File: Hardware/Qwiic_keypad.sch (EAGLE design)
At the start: 26 parts, among them J3 PTH, J6 AVR_SPI_PROG_3X2TESTPOINTS, U3 ATTINY84

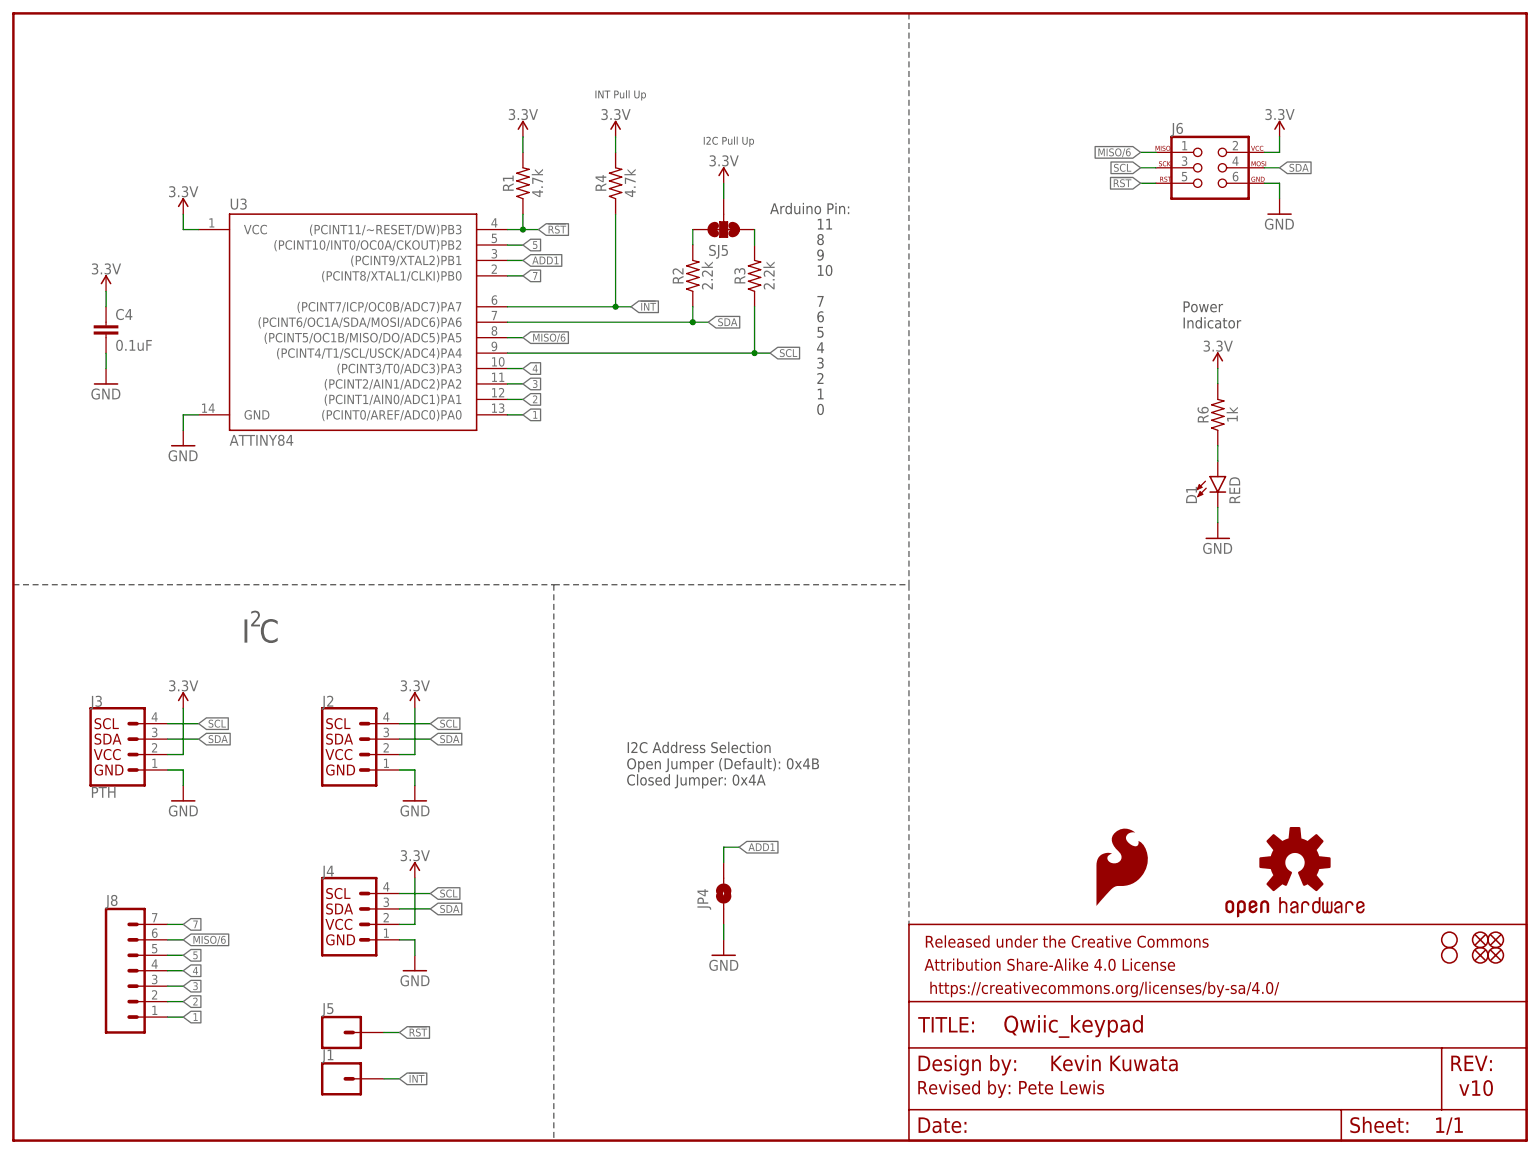
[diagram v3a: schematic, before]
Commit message: hardware review changes
beef up trace to 3.3V PTH header breakout as well.
Nudged I2C label up to match power label hieght.
ATTINY84 polarity mark fill in library
Logo up to .2 size flame.
Schematic note for I2C pullup jumper
Updated ATTiny device (just the symbol changed, but needed to "replace" due to new pin names).
nudged LED lower to ensure mask gap from nearby resistor
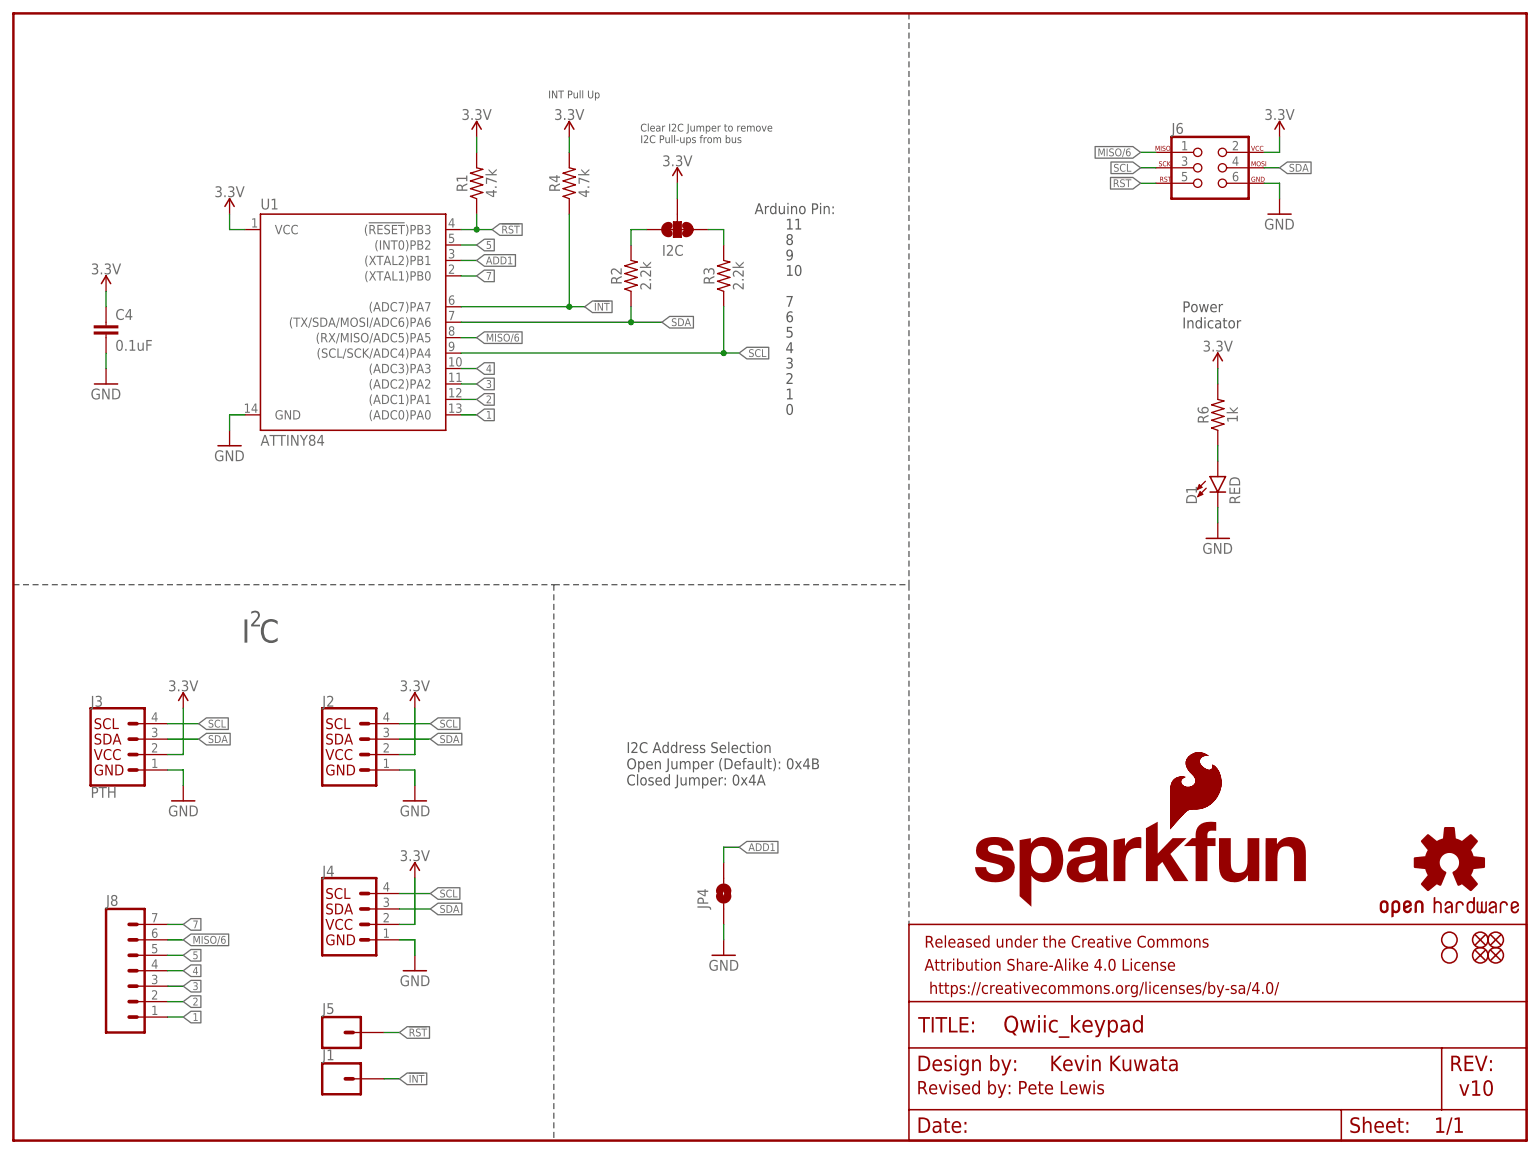
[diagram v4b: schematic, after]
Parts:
- removed SJ5: JUMPER-SMT_3_2-NC_TRACE_SILK, SparkFun-Jumpers:JUMPER-SMT_3_2-NC_TRACE_SILK
- removed U3: ATTINY84, SparkFun-IC-Microcontroller:ATTINY84
- added I2C: JUMPER-SMT_3_2-NC_TRACE_SILK, SparkFun-Jumpers:JUMPER-SMT_3_2-NC_TRACE_SILK
- added LOGO2: SFE_LOGO_NAME_FLAME.1_INCH, SparkFun-Aesthetics:SFE_LOGO_NAME_FLAME.1_INCH
- added U1: ATTINY84, SparkFun-IC-Microcontroller:ATTINY84
- LOGO3: value SFE_LOGO_FLAME.1_INCH -> SFE_LOGO_FLAME.2_INCH; device SparkFun-Aesthetics:SFE_LOGO_FLAME.1_INCH -> SparkFun-Aesthetics:SFE_LOGO_FLAME.2_INCH
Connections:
- net !INT: now also U1.(ADC7)PA7; no longer U3.(PCINT7/ICP/OC0B/ADC7)PA7
- net !RST: now also U1.(!RESET!)PB3; no longer U3.(PCINT11/~RESET/DW)PB3
- net 1: now also U1.(ADC0)PA0; no longer U3.(PCINT0/AREF/ADC0)PA0
- net 2: now also U1.(ADC1)PA1; no longer U3.(PCINT1/AIN0/ADC1)PA1
- net 3: now also U1.(ADC2)PA2; no longer U3.(PCINT2/AIN1/ADC2)PA2
- net 3.3V: now also I2C.2, U1.VCC; no longer SJ5.2, U3.VCC
- net 4: now also U1.(ADC3)PA3; no longer U3.(PCINT3/T0/ADC3)PA3
- net 5: now also U1.(INT0)PB2; no longer U3.(PCINT10/INT0/OC0A/CKOUT)PB2
- net 7: now also U1.(XTAL1)PB0; no longer U3.(PCINT8/XTAL1/CLKI)PB0
- net ADD1: now also U1.(XTAL2)PB1; no longer U3.(PCINT9/XTAL2)PB1
- net GND: now also U1.GND; no longer U3.GND
- net MISO/6: now also U1.(RX/MISO/ADC5)PA5; no longer U3.(PCINT5/OC1B/MISO/DO/ADC5)PA5
- net N$2: now also I2C.3; no longer SJ5.3
- net N$3: now also I2C.1; no longer SJ5.1
- net SCL: now also U1.(SCL/SCK/ADC4)PA4; no longer U3.(PCINT4/T1/SCL/USCK/ADC4)PA4
- net SDA: now also U1.(TX/SDA/MOSI/ADC6)PA6; no longer U3.(PCINT6/OC1A/SDA/MOSI/ADC6)PA6
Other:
- note added: "Clear I2C Jumper to remove I2C Pull-ups from bus"
- note removed: "I2C Pull Up"
- moved on the sheet: R1, R2, R3, R4

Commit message: double-check (my run) fixes
added SS path on 48.
package update on address jumper - to 8 mil width on silk outline.
library update to SFE library on I2C jumper (was sparkx lbr).
some minor routing tweaks to allow more gnd flow
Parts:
- J3: device SparkX:I2C_STANDARD_NO_SILK -> SparkFun-Connectors:I2C_STANDARD_NO_SILK
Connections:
- net 3.3V: now also J3.2; no longer J3.VCC
- net GND: now also J3.1; no longer J3.GND
- net SCL: now also J3.4; no longer J3.SCL
- net SDA: now also J3.3; no longer J3.SDA
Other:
- note added: "ATTiny84"
- note added: "I2C Connections"
- note added: "Keypad Connections"
- note added: "Pogo Programmer"
- note added: "Vin: 2.7-5.5V"
- note added: "WARNING: Use only 3.3V when connecting multiple qwiic boards."
- note removed: "I C"
- moved on the sheet: D1, J1, J2, J3, J4, J5, J8, JP4, R6
